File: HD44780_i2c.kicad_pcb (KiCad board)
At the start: 2 copper layers, 23 x 48 mm, 13 parts, among them IC1 TCA6416APWR, J1 Conn_01x05_Male, J2 Conn_01x02_Male, J3 Conn_01x05, J4 Conn_01x18_Male, Q1 Q_NPN_BCE

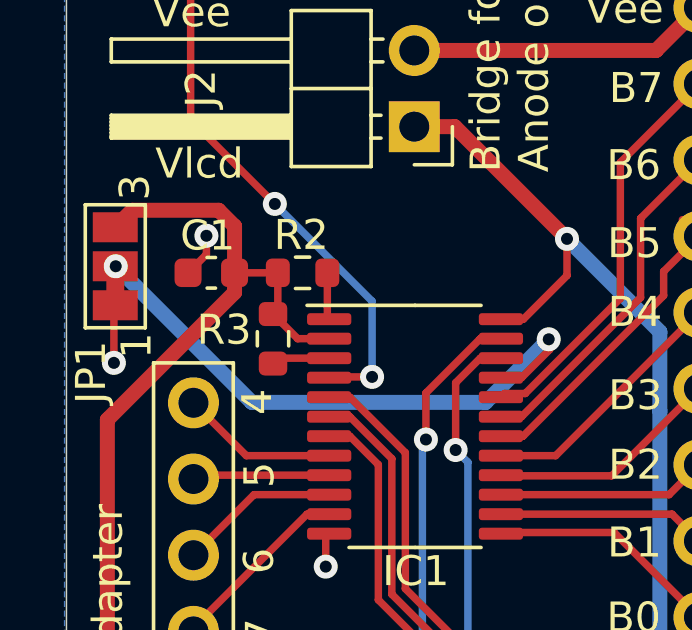
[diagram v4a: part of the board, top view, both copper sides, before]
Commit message: Improve clearance between address pad and components.
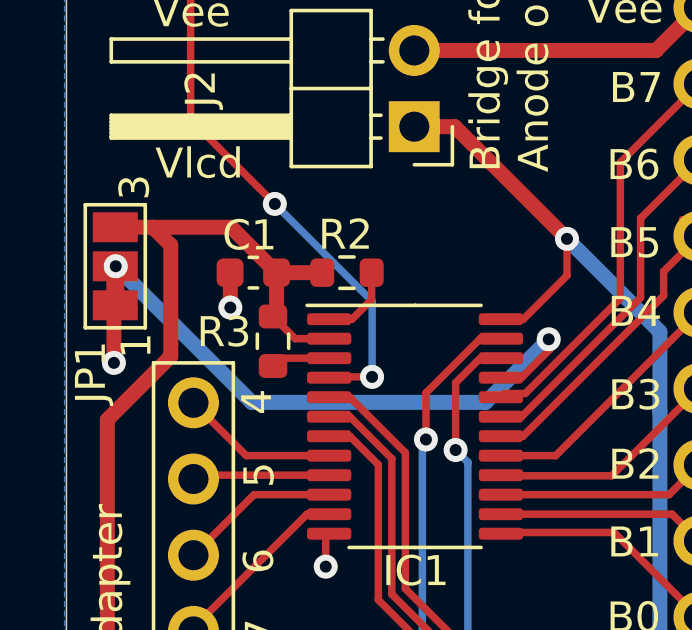
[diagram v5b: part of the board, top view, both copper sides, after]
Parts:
- moved R2 1.48 mm to (159.3, 91.3)
- moved C1 1.40 mm to (156.2, 91.3)
- moved R3 0.08 mm to (156.9, 93.6)
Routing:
- net VDD: track 55.0 -> 56.1 mm
- net Net-(IC1-Pad1): track 1.57 -> 2.58 mm
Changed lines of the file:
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@@
     (thickness 1.6)
     (drawings 42)
-    (tracks 158)
+    (tracks 159)
     (zones 0)
     (modules 13)
@@
   )
   (module Resistor_SMD:R_0603_1608Metric (layer F.Cu)
-    (at 156.88564 93.51264 90)
+    (at 156.88564 93.59392 90)
     (descr "Resistor SMD 0603 (1608 Metric), square (rectangular) end terminal, IPC_7351 nominal, (Body size source: IPC-SM-782 page 72, https://www.pcb-3d.com/wordpress/wp-content/uploads/ipc-sm-782a_amendment_1_and_2.pdf), generated with kicad-footprint-generator")
     (tags resistor)
@@
   )
   (module Resistor_SMD:R_0603_1608Metric (layer F.Cu)
-    (at 157.87116 91.313 180)
+    (at 159.34944 91.30792 180)
     (descr "Resistor SMD 0603 (1608 Metric), square (rectangular) end terminal, IPC_7351 nominal, (Body size source: IPC-SM-782 page 72, https://www.pcb-3d.com/wordpress/wp-content/uploads/ipc-sm-782a_amendment_1_and_2.pdf), generated with kicad-footprint-generator")
     (tags resistor)
@@
   )
   (module Capacitor_SMD:C_0603_1608Metric (layer F.Cu)
-    (at 154.82824 91.313 180)
+    (at 156.23032 91.30792 180)
     (descr "Capacitor SMD 0603 (1608 Metric), square (rectangular) end terminal, IPC_7351 nominal, (Body size source: IPC-SM-782 page 76, https://www.pcb-3d.com/wordpress/wp-content/uploads/ipc-sm-782a_amendment_1_and_2.pdf), generated with kicad-footprint-generator")
     (tags capacitor)
@@
   (segment (start 169.97598 116.92808) (end 171.0817 118.0338) (width 0.5) (layer F.Cu) (net 1))
   (segment (start 167.98736 116.92808) (end 169.97598 116.92808) (width 0.5) (layer F.Cu) (net 1))
-  (via (at 154.66568 90.07856) (size 0.8) (drill 0.4) (layers F.Cu B.Cu) (net 1))
-  (segment (start 154.66568 90.70056) (end 154.05324 91.313) (width 0.25) (layer F.Cu) (net 1))
-  (segment (start 154.66568 90.07856) (end 154.66568 90.70056) (width 0.25) (layer F.Cu) (net 1))
   (via (at 158.64332 101.10724) (size 0.8) (drill 0.4) (layers F.Cu B.Cu) (net 1))
   (segment (start 158.64332 100.12302) (end 158.7577 100.00864) (width 0.25) (layer F.Cu) (net 1))
   (segment (start 158.64332 101.10724) (end 158.64332 100.12302) (width 0.25) (layer F.Cu) (net 1))
   (via (at 151.58212 94.31528) (size 0.8) (drill 0.4) (layers F.Cu B.Cu) (net 1))
-  (segment (start 151.58212 92.44028) (end 151.62784 92.39456) (width 0.25) (layer F.Cu) (net 1))
-  (segment (start 151.58212 94.31528) (end 151.58212 92.44028) (width 0.25) (layer F.Cu) (net 1))
-  (segment (start 157.04616 92.52712) (end 156.88564 92.68764) (width 0.25) (layer F.Cu) (net 28))
-  (segment (start 157.04616 91.313) (end 157.04616 92.52712) (width 0.25) (layer F.Cu) (net 28))
-  (segment (start 157.70664 93.50864) (end 158.7577 93.50864) (width 0.25) (layer F.Cu) (net 28))
-  (segment (start 156.88564 92.68764) (end 157.70664 93.50864) (width 0.25) (layer F.Cu) (net 28))
-  (segment (start 155.60324 91.313) (end 157.04616 91.313) (width 0.25) (layer F.Cu) (net 28))
+  (via (at 155.46324 92.47124) (size 0.8) (drill 0.4) (layers F.Cu B.Cu) (net 1))
+  (segment (start 155.46324 91.31584) (end 155.45532 91.30792) (width 0.5) (layer F.Cu) (net 1))
+  (segment (start 155.46324 92.47124) (end 155.46324 91.31584) (width 0.5) (layer F.Cu) (net 1))
+  (segment (start 151.58212 92.44028) (end 151.62784 92.39456) (width 0.5) (layer F.Cu) (net 1))
+  (segment (start 151.58212 94.31528) (end 151.58212 92.44028) (width 0.5) (layer F.Cu) (net 1))
   (segment (start 161.0741 120.6627) (end 161.0741 122.5423) (width 0.5) (layer F.Cu) (net 28))
   (segment (start 161.0741 122.5423) (end 160.49752 123.11888) (width 0.5) (layer F.Cu) (net 28))
   (segment (start 160.49752 123.11888) (end 153.80716 123.11888) (width 0.5) (layer F.Cu) (net 28))
   (segment (start 153.80716 123.11888) (end 151.36368 120.6754) (width 0.5) (layer F.Cu) (net 28))
-  (segment (start 155.60324 91.97056) (end 151.36368 96.21012) (width 0.5) (layer F.Cu) (net 28))
-  (segment (start 155.60324 91.313) (end 155.60324 91.97056) (width 0.5) (layer F.Cu) (net 28))
   (segment (start 151.36368 120.6754) (end 151.36368 96.21012) (width 0.5) (layer F.Cu) (net 28))
-  (segment (start 155.60324 89.758118) (end 155.60324 91.313) (width 0.5) (layer F.Cu) (net 28))
-  (segment (start 155.073681 89.228559) (end 155.60324 89.758118) (width 0.5) (layer F.Cu) (net 28))
-  (segment (start 152.193841 89.228559) (end 155.073681 89.228559) (width 0.5) (layer F.Cu) (net 28))
-  (segment (start 151.62784 89.79456) (end 152.193841 89.228559) (width 0.5) (layer F.Cu) (net 28))
   (segment (start 159.72872 116.92808) (end 165.68736 116.92808) (width 0.5) (layer F.Cu) (net 2))
   (segment (start 155.9941 120.6627) (end 159.72872 116.92808) (width 0.5) (layer F.Cu) (net 2))
@@
   (segment (start 158.7837 94.78264) (end 158.7577 94.80864) (width 0.25) (layer F.Cu) (net 21))
   (segment (start 160.18764 94.78264) (end 158.7837 94.78264) (width 0.25) (layer F.Cu) (net 21))
-  (segment (start 157.06464 94.15864) (end 158.7577 94.15864) (width 0.25) (layer F.Cu) (net 22))
-  (segment (start 156.88564 94.33764) (end 157.06464 94.15864) (width 0.25) (layer F.Cu) (net 22))
-  (segment (start 158.69616 92.7971) (end 158.7577 92.85864) (width 0.25) (layer F.Cu) (net 23))
-  (segment (start 158.69616 91.313) (end 158.69616 92.7971) (width 0.25) (layer F.Cu) (net 23))
+  (segment (start 157.14592 94.15864) (end 156.88564 94.41892) (width 0.25) (layer F.Cu) (net 22))
+  (segment (start 158.7577 94.15864) (end 157.14592 94.15864) (width 0.25) (layer F.Cu) (net 22))
+  (segment (start 160.17444 91.30792) (end 160.17444 92.20504) (width 0.25) (layer F.Cu) (net 23))
+  (segment (start 159.52084 92.85864) (end 158.7577 92.85864) (width 0.25) (layer F.Cu) (net 23))
+  (segment (start 160.17444 92.20504) (end 159.52084 92.85864) (width 0.25) (layer F.Cu) (net 23))
   (segment (start 168.36308 112.9538) (end 166.83736 111.42808) (width 0.5) (layer F.Cu) (net 24))
   (segment (start 171.0817 112.9538) (end 168.36308 112.9538) (width 0.5) (layer F.Cu) (net 24))
@@
   (segment (start 172.381701 119.273799) (end 172.381701 81.233801) (width 0.5) (layer F.Cu) (net 27))
   (segment (start 171.0817 120.5738) (end 172.381701 119.273799) (width 0.5) (layer F.Cu) (net 27))
+  (segment (start 157.62536 93.50864) (end 156.88564 92.76892) (width 0.25) (layer F.Cu) (net 28))
+  (segment (start 158.7577 93.50864) (end 157.62536 93.50864) (width 0.25) (layer F.Cu) (net 28))
+  (segment (start 152.87784 89.79456) (end 151.62784 89.79456) (width 0.5) (layer F.Cu) (net 28))
+  (segment (start 153.47696 90.39368) (end 152.87784 89.79456) (width 0.5) (layer F.Cu) (net 28))
+  (segment (start 153.47696 94.09684) (end 153.47696 90.39368) (width 0.5) (layer F.Cu) (net 28))
+  (segment (start 151.36368 96.21012) (end 153.47696 94.09684) (width 0.5) (layer F.Cu) (net 28))
+  (segment (start 157.00532 91.30792) (end 158.52444 91.30792) (width 0.5) (layer F.Cu) (net 28))
+  (segment (start 157.00532 92.64924) (end 156.88564 92.76892) (width 0.5) (layer F.Cu) (net 28))
+  (segment (start 157.00532 91.30792) (end 157.00532 92.64924) (width 0.5) (layer F.Cu) (net 28))
+  (segment (start 155.49196 89.79456) (end 152.87784 89.79456) (width 0.5) (layer F.Cu) (net 28))
+  (segment (start 157.00532 91.30792) (end 155.49196 89.79456) (width 0.5) (layer F.Cu) (net 28))
   (zone (net 1) (net_name GND) (layer B.Cu) (hatch edge 0.508)
     (connect_pads (clearance 0.508))

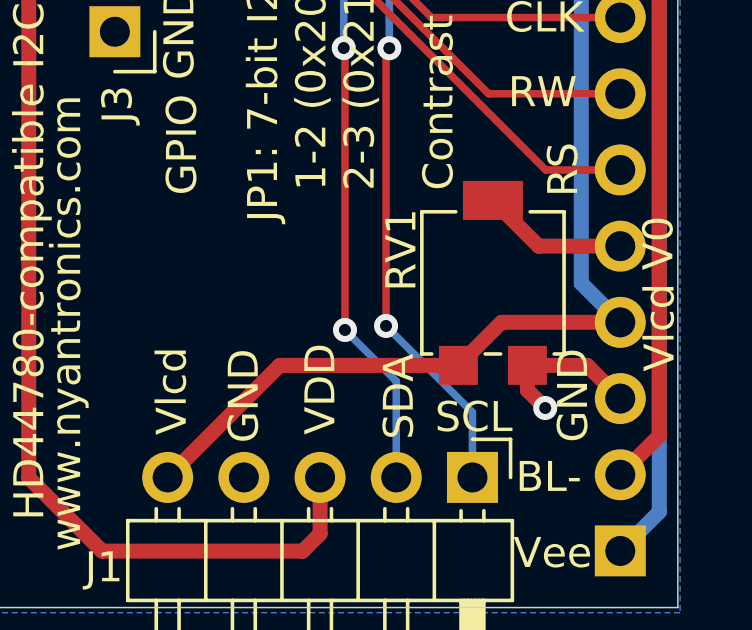
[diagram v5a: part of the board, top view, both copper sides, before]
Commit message: Replace trimmer with most cost-effective variant.
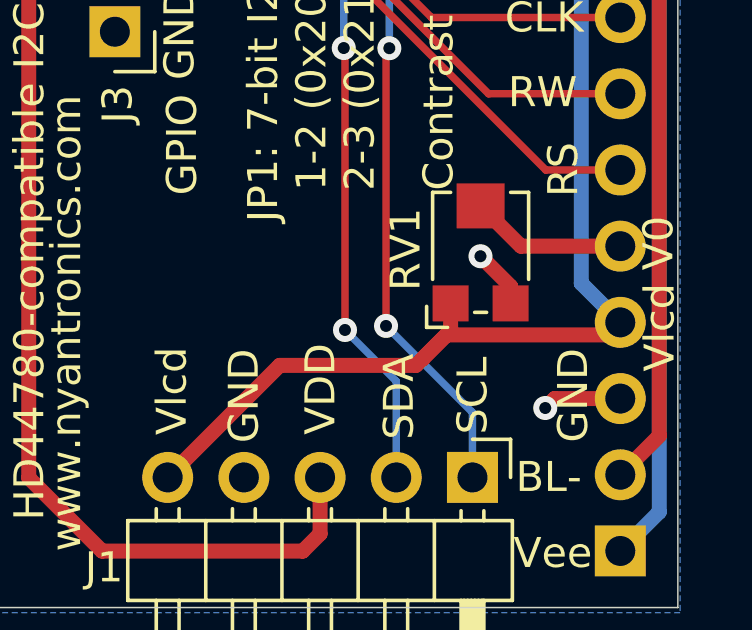
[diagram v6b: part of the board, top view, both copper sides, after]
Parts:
- removed G***: LOGO, kicad_art:nyantronics_logo
- RV1: footprint Potentiometer_SMD:Potentiometer_Bourns_3314G_Vertical -> Potentiometer_SMD:Potentiometer_Bourns_TC33X_Vertical
- moved RV1 1.19 mm to (166.4, 113.1), turned to 90 degrees
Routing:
- net Vlcd: track 55.0 -> 57.3 mm
- net GND: track 10.9 -> 10.3 mm, vias 5 -> 6

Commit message: Update BL cathode naming and schematic comments.
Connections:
- net GND_bl renamed BLK
